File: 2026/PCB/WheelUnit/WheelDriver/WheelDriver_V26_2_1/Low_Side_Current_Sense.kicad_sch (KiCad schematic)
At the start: 4 parts

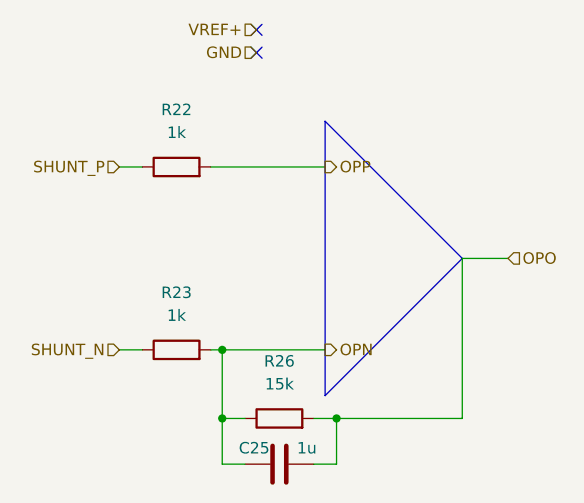
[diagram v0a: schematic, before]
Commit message: FETの回路記号間違ってた
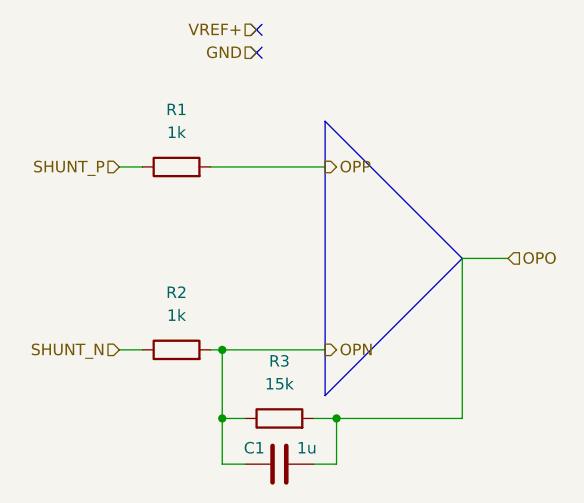
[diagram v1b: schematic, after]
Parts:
- renumbered C25 to C1, R22 to R1, R23 to R2, R26 to R3

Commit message: 回路図4ch化
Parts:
- renumbered R2 to R10, R3 to R11, R1 to R9
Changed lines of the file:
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@@
 		(dnp no)
 		(fields_autoplaced yes)
-		(property "Reference" "R3"
+		(property "Reference" "R11"
 			(at 52.07 60.96 90)
 			(effects
@@
 			(project "WheelDriver_V26_2_1"
 				(path "/b60d34e1-e978-4abb-befd-6af7b603dc53/01c53688-c3c5-4098-8cb1-7076c72bfd6c/1754fd9d-f06d-4a63-8106-0e516498ff0d"
-					(reference "R9")
+					(reference "R17")
 					(unit 1)
 				)
 				(path "/b60d34e1-e978-4abb-befd-6af7b603dc53/01c53688-c3c5-4098-8cb1-7076c72bfd6c/226df0eb-272b-4d8a-9e6a-d196eca276c9"
-					(reference "R3")
+					(reference "R11")
 					(unit 1)
 				)
 				(path "/b60d34e1-e978-4abb-befd-6af7b603dc53/01c53688-c3c5-4098-8cb1-7076c72bfd6c/936d36b9-b6a7-4b30-9ebf-106de9ae1b9f"
-					(reference "R6")
+					(reference "R14")
+					(unit 1)
+				)
+				(path "/b60d34e1-e978-4abb-befd-6af7b603dc53/1a3a8f6e-480e-480c-9983-0b0013ec66fb/1754fd9d-f06d-4a63-8106-0e516498ff0d"
+					(reference "R118")
+					(unit 1)
+				)
+				(path "/b60d34e1-e978-4abb-befd-6af7b603dc53/1a3a8f6e-480e-480c-9983-0b0013ec66fb/226df0eb-272b-4d8a-9e6a-d196eca276c9"
+					(reference "R124")
+					(unit 1)
+				)
+				(path "/b60d34e1-e978-4abb-befd-6af7b603dc53/1a3a8f6e-480e-480c-9983-0b0013ec66fb/936d36b9-b6a7-4b30-9ebf-106de9ae1b9f"
+					(reference "R121")
+					(unit 1)
+				)
+				(path "/b60d34e1-e978-4abb-befd-6af7b603dc53/2a825334-bae1-4595-a946-248e1aa4e7b3/1754fd9d-f06d-4a63-8106-0e516498ff0d"
+					(reference "R89")
+					(unit 1)
+				)
+				(path "/b60d34e1-e978-4abb-befd-6af7b603dc53/2a825334-bae1-4595-a946-248e1aa4e7b3/226df0eb-272b-4d8a-9e6a-d196eca276c9"
+					(reference "R95")
+					(unit 1)
+				)
+				(path "/b60d34e1-e978-4abb-befd-6af7b603dc53/2a825334-bae1-4595-a946-248e1aa4e7b3/936d36b9-b6a7-4b30-9ebf-106de9ae1b9f"
+					(reference "R92")
+					(unit 1)
+				)
+				(path "/b60d34e1-e978-4abb-befd-6af7b603dc53/49f48e62-539f-411b-8925-0b0084105390/1754fd9d-f06d-4a63-8106-0e516498ff0d"
+					(reference "R60")
+					(unit 1)
+				)
+				(path "/b60d34e1-e978-4abb-befd-6af7b603dc53/49f48e62-539f-411b-8925-0b0084105390/226df0eb-272b-4d8a-9e6a-d196eca276c9"
+					(reference "R66")
+					(unit 1)
+				)
+				(path "/b60d34e1-e978-4abb-befd-6af7b603dc53/49f48e62-539f-411b-8925-0b0084105390/936d36b9-b6a7-4b30-9ebf-106de9ae1b9f"
+					(reference "R63")
 					(unit 1)
 				)
@@
 					(unit 1)
 				)
+				(path "/b60d34e1-e978-4abb-befd-6af7b603dc53/1a3a8f6e-480e-480c-9983-0b0013ec66fb/1754fd9d-f06d-4a63-8106-0e516498ff0d"
+					(reference "C122")
+					(unit 1)
+				)
+				(path "/b60d34e1-e978-4abb-befd-6af7b603dc53/1a3a8f6e-480e-480c-9983-0b0013ec66fb/226df0eb-272b-4d8a-9e6a-d196eca276c9"
+					(reference "C124")
+					(unit 1)
+				)
+				(path "/b60d34e1-e978-4abb-befd-6af7b603dc53/1a3a8f6e-480e-480c-9983-0b0013ec66fb/936d36b9-b6a7-4b30-9ebf-106de9ae1b9f"
+					(reference "C123")
+					(unit 1)
+				)
+				(path "/b60d34e1-e978-4abb-befd-6af7b603dc53/2a825334-bae1-4595-a946-248e1aa4e7b3/1754fd9d-f06d-4a63-8106-0e516498ff0d"
+					(reference "C91")
+					(unit 1)
+				)
+				(path "/b60d34e1-e978-4abb-befd-6af7b603dc53/2a825334-bae1-4595-a946-248e1aa4e7b3/226df0eb-272b-4d8a-9e6a-d196eca276c9"
+					(reference "C93")
+					(unit 1)
+				)
+				(path "/b60d34e1-e978-4abb-befd-6af7b603dc53/2a825334-bae1-4595-a946-248e1aa4e7b3/936d36b9-b6a7-4b30-9ebf-106de9ae1b9f"
+					(reference "C92")
+					(unit 1)
+				)
+				(path "/b60d34e1-e978-4abb-befd-6af7b603dc53/49f48e62-539f-411b-8925-0b0084105390/1754fd9d-f06d-4a63-8106-0e516498ff0d"
+					(reference "C60")
+					(unit 1)
+				)
+				(path "/b60d34e1-e978-4abb-befd-6af7b603dc53/49f48e62-539f-411b-8925-0b0084105390/226df0eb-272b-4d8a-9e6a-d196eca276c9"
+					(reference "C62")
+					(unit 1)
+				)
+				(path "/b60d34e1-e978-4abb-befd-6af7b603dc53/49f48e62-539f-411b-8925-0b0084105390/936d36b9-b6a7-4b30-9ebf-106de9ae1b9f"
+					(reference "C61")
+					(unit 1)
+				)
 			)
 		)
@@
 		(dnp no)
 		(fields_autoplaced yes)
-		(property "Reference" "R2"
+		(property "Reference" "R10"
 			(at 40.64 53.34 90)
 			(effects
@@
 			(project "WheelDriver_V26_2_1"
 				(path "/b60d34e1-e978-4abb-befd-6af7b603dc53/01c53688-c3c5-4098-8cb1-7076c72bfd6c/1754fd9d-f06d-4a63-8106-0e516498ff0d"
-					(reference "R8")
+					(reference "R16")
 					(unit 1)
 				)
 				(path "/b60d34e1-e978-4abb-befd-6af7b603dc53/01c53688-c3c5-4098-8cb1-7076c72bfd6c/226df0eb-272b-4d8a-9e6a-d196eca276c9"
-					(reference "R2")
+					(reference "R10")
 					(unit 1)
 				)
 				(path "/b60d34e1-e978-4abb-befd-6af7b603dc53/01c53688-c3c5-4098-8cb1-7076c72bfd6c/936d36b9-b6a7-4b30-9ebf-106de9ae1b9f"
-					(reference "R5")
+					(reference "R13")
+					(unit 1)
+				)
+				(path "/b60d34e1-e978-4abb-befd-6af7b603dc53/1a3a8f6e-480e-480c-9983-0b0013ec66fb/1754fd9d-f06d-4a63-8106-0e516498ff0d"
+					(reference "R117")
+					(unit 1)
+				)
+				(path "/b60d34e1-e978-4abb-befd-6af7b603dc53/1a3a8f6e-480e-480c-9983-0b0013ec66fb/226df0eb-272b-4d8a-9e6a-d196eca276c9"
+					(reference "R123")
+					(unit 1)
+				)
+				(path "/b60d34e1-e978-4abb-befd-6af7b603dc53/1a3a8f6e-480e-480c-9983-0b0013ec66fb/936d36b9-b6a7-4b30-9ebf-106de9ae1b9f"
+					(reference "R120")
+					(unit 1)
+				)
+				(path "/b60d34e1-e978-4abb-befd-6af7b603dc53/2a825334-bae1-4595-a946-248e1aa4e7b3/1754fd9d-f06d-4a63-8106-0e516498ff0d"
+					(reference "R88")
+					(unit 1)
+				)
+				(path "/b60d34e1-e978-4abb-befd-6af7b603dc53/2a825334-bae1-4595-a946-248e1aa4e7b3/226df0eb-272b-4d8a-9e6a-d196eca276c9"
+					(reference "R94")
+					(unit 1)
+				)
+				(path "/b60d34e1-e978-4abb-befd-6af7b603dc53/2a825334-bae1-4595-a946-248e1aa4e7b3/936d36b9-b6a7-4b30-9ebf-106de9ae1b9f"
+					(reference "R91")
+					(unit 1)
+				)
+				(path "/b60d34e1-e978-4abb-befd-6af7b603dc53/49f48e62-539f-411b-8925-0b0084105390/1754fd9d-f06d-4a63-8106-0e516498ff0d"
+					(reference "R59")
+					(unit 1)
+				)
+				(path "/b60d34e1-e978-4abb-befd-6af7b603dc53/49f48e62-539f-411b-8925-0b0084105390/226df0eb-272b-4d8a-9e6a-d196eca276c9"
+					(reference "R65")
+					(unit 1)
+				)
+				(path "/b60d34e1-e978-4abb-befd-6af7b603dc53/49f48e62-539f-411b-8925-0b0084105390/936d36b9-b6a7-4b30-9ebf-106de9ae1b9f"
+					(reference "R62")
 					(unit 1)
 				)
@@
 		(dnp no)
 		(fields_autoplaced yes)
-		(property "Reference" "R1"
+		(property "Reference" "R9"
 			(at 40.64 33.02 90)
 			(effects
@@
 			(project "WheelDriver_V26_2_1"
 				(path "/b60d34e1-e978-4abb-befd-6af7b603dc53/01c53688-c3c5-4098-8cb1-7076c72bfd6c/1754fd9d-f06d-4a63-8106-0e516498ff0d"
-					(reference "R7")
+					(reference "R15")
 					(unit 1)
 				)
 				(path "/b60d34e1-e978-4abb-befd-6af7b603dc53/01c53688-c3c5-4098-8cb1-7076c72bfd6c/226df0eb-272b-4d8a-9e6a-d196eca276c9"
-					(reference "R1")
+					(reference "R9")
 					(unit 1)
 				)
 				(path "/b60d34e1-e978-4abb-befd-6af7b603dc53/01c53688-c3c5-4098-8cb1-7076c72bfd6c/936d36b9-b6a7-4b30-9ebf-106de9ae1b9f"
-					(reference "R4")
-					(unit 1)
-				)
+					(reference "R12")
+					(unit 1)
+				)
+				(path "/b60d34e1-e978-4abb-befd-6af7b603dc53/1a3a8f6e-480e-480c-9983-0b0013ec66fb/1754fd9d-f06d-4a63-8106-0e516498ff0d"
+					(reference "R116")
+					(unit 1)
+				)
+				(path "/b60d34e1-e978-4abb-befd-6af7b603dc53/1a3a8f6e-480e-480c-9983-0b0013ec66fb/226df0eb-272b-4d8a-9e6a-d196eca276c9"
+					(reference "R122")
+					(unit 1)
+				)
+				(path "/b60d34e1-e978-4abb-befd-6af7b603dc53/1a3a8f6e-480e-480c-9983-0b0013ec66fb/936d36b9-b6a7-4b30-9ebf-106de9ae1b9f"
+					(reference "R119")
+					(unit 1)
+				)
+				(path "/b60d34e1-e978-4abb-befd-6af7b603dc53/2a825334-bae1-4595-a946-248e1aa4e7b3/1754fd9d-f06d-4a63-8106-0e516498ff0d"
+					(reference "R87")
+					(unit 1)
+				)
+				(path "/b60d34e1-e978-4abb-befd-6af7b603dc53/2a825334-bae1-4595-a946-248e1aa4e7b3/226df0eb-272b-4d8a-9e6a-d196eca276c9"
+					(reference "R93")
+					(unit 1)
+				)
+				(path "/b60d34e1-e978-4abb-befd-6af7b603dc53/2a825334-bae1-4595-a946-248e1aa4e7b3/936d36b9-b6a7-4b30-9ebf-106de9ae1b9f"
+					(reference "R90")
+					(unit 1)
+				)
+				(path "/b60d34e1-e978-4abb-befd-6af7b603dc53/49f48e62-539f-411b-8925-0b0084105390/1754fd9d-f06d-4a63-8106-0e516498ff0d"
+					(reference "R58")
+					(unit 1)
+				)
+				(path "/b60d34e1-e978-4abb-befd-6af7b603dc53/49f48e62-539f-411b-8925-0b0084105390/226df0eb-272b-4d8a-9e6a-d196eca276c9"
+					(reference "R64")
+					(unit 1)
+				)
+				(path "/b60d34e1-e978-4abb-befd-6af7b603dc53/49f48e62-539f-411b-8925-0b0084105390/936d36b9-b6a7-4b30-9ebf-106de9ae1b9f"
+					(reference "R61")
+					(unit 1)
+				)

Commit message: PCBアートワーク完了
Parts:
- R11: value 15k -> 180k
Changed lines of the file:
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@@
 			)
 		)
-		(property "Value" "15k"
+		(property "Value" "180k"
 			(at 52.07 63.5 90)
 			(effects
